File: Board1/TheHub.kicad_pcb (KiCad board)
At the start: 2 copper layers, 118.7 x 184.1 mm, 51 parts, among them J11 RFD900, J12 I2C_1 Test Point, J13 I2C_2 Test Point, J15 GPIO Test, J16 I2C_3 Test Point, J17 12V OUT, J23 NucleoRight, J5 NucleoLeft, J8 12V MAIN POWER, U10 ADXL377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

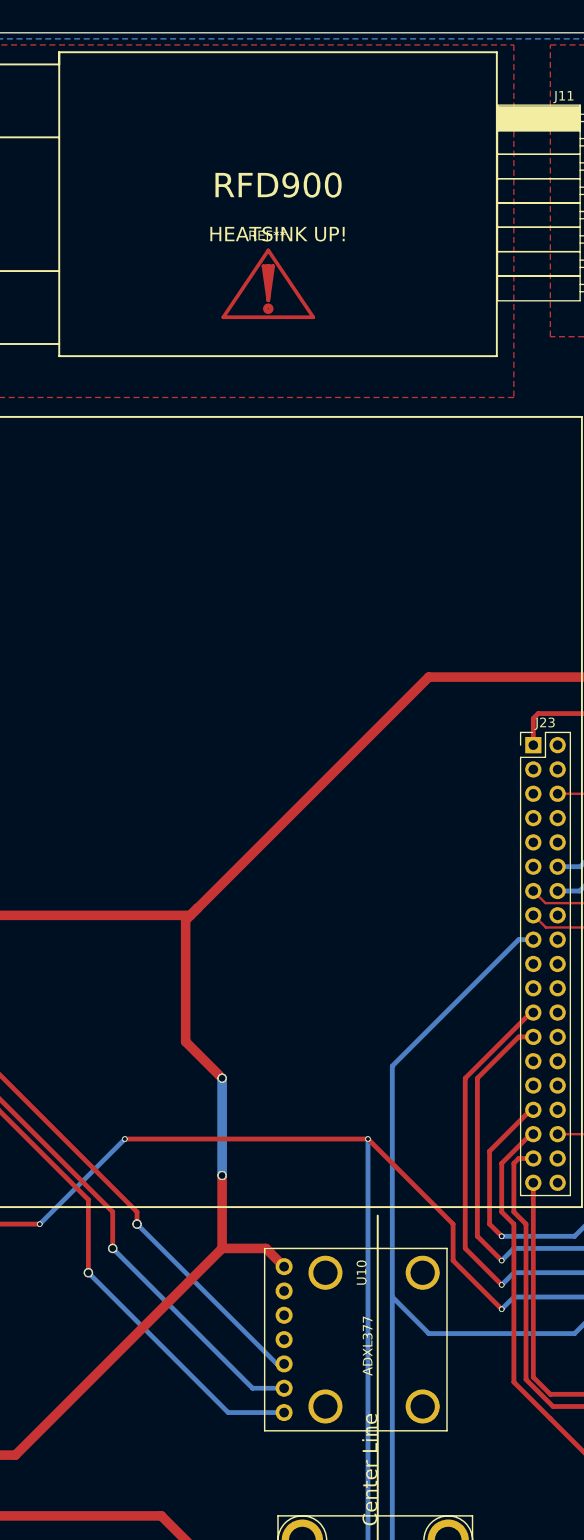
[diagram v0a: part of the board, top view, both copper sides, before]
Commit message: Add mounting points for RFD900
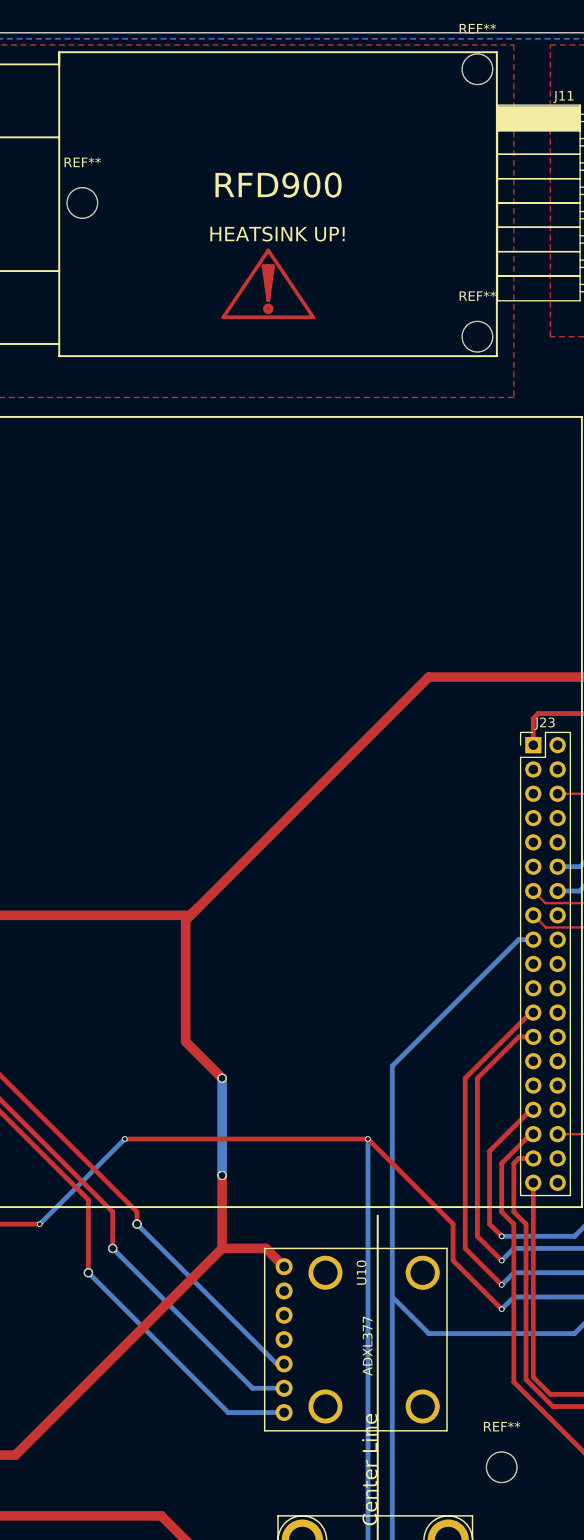
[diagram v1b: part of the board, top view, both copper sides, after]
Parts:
- added REF**: MountingHole_3.2mm_M3, Mounting_Holes:MountingHole_3.2mm_M3, F.Cu at (134.6, 200.7)
- added REF**: MountingHole_3.2mm_M3, Mounting_Holes:MountingHole_3.2mm_M3, F.Cu at (132.1, 82.5)
- added REF**: MountingHole_3.2mm_M3, Mounting_Holes:MountingHole_3.2mm_M3, F.Cu at (132.1, 54.6)
- added REF**: MountingHole_3.2mm_M3, Mounting_Holes:MountingHole_3.2mm_M3, F.Cu at (90.8, 68.6)
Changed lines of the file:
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@@
     (tracks 318)
     (zones 0)
-    (modules 51)
+    (modules 55)
     (nets 107)
   )
@@
     (descr "Symbol, Attention, Copper Top, Small,")
     (tags "Symbol, Attention, Copper Top, Small,")
-    (fp_text reference REF** (at -0.127 -5.715) (layer F.SilkS)
+    (fp_text reference REF** (at 9.144 2.921) (layer F.SilkS) hide
       (effects (font (size 1 1) (thickness 0.15)))
     )
@@
     (pad "" thru_hole circle (at 12.7 -10.16 90) (size 3.5 3.5) (drill 2.55) (layers *.Cu *.Mask))
   )
+  (module Mounting_Holes:MountingHole_3.2mm_M3 (layer F.Cu)
+    (at 134.62 200.66)
+    (descr "Mounting Hole 3.2mm, no annular, M3")
+    (tags "mounting hole 3.2mm no annular m3")
+    (attr virtual)
+    (fp_text reference REF** (at 0 -4.2) (layer F.SilkS)
+      (effects (font (size 1 1) (thickness 0.15)))
+    )
+    (fp_text value MountingHole_3.2mm_M3 (at 0 4.2) (layer F.Fab)
+      (effects (font (size 1 1) (thickness 0.15)))
+    )
+    (fp_text user %R (at 0.3 0) (layer F.Fab)
+      (effects (font (size 1 1) (thickness 0.15)))
+    )
+    (fp_circle (center 0 0) (end 3.2 0) (layer Cmts.User) (width 0.15))
+    (fp_circle (center 0 0) (end 3.45 0) (layer F.CrtYd) (width 0.05))
+    (pad 1 np_thru_hole circle (at 0 0) (size 3.2 3.2) (drill 3.2) (layers *.Cu *.Mask))
+  )
+  (module Mounting_Holes:MountingHole_3.2mm_M3 (layer F.Cu)
+    (at 132.08 82.55)
+    (descr "Mounting Hole 3.2mm, no annular, M3")
+    (tags "mounting hole 3.2mm no annular m3")
+    (attr virtual)
+    (fp_text reference REF** (at 0 -4.2) (layer F.SilkS)
+      (effects (font (size 1 1) (thickness 0.15)))
+    )
+    (fp_text value MountingHole_3.2mm_M3 (at 0 4.2) (layer F.Fab)
+      (effects (font (size 1 1) (thickness 0.15)))
+    )
+    (fp_text user %R (at 0.3 0) (layer F.Fab)
+      (effects (font (size 1 1) (thickness 0.15)))
+    )
+    (fp_circle (center 0 0) (end 3.2 0) (layer Cmts.User) (width 0.15))
+    (fp_circle (center 0 0) (end 3.45 0) (layer F.CrtYd) (width 0.05))
+    (pad 1 np_thru_hole circle (at 0 0) (size 3.2 3.2) (drill 3.2) (layers *.Cu *.Mask))
+  )
+  (module Mounting_Holes:MountingHole_3.2mm_M3 (layer F.Cu)
+    (at 132.08 54.61)
+    (descr "Mounting Hole 3.2mm, no annular, M3")
+    (tags "mounting hole 3.2mm no annular m3")
+    (attr virtual)
+    (fp_text reference REF** (at 0 -4.2) (layer F.SilkS)
+      (effects (font (size 1 1) (thickness 0.15)))
+    )
+    (fp_text value MountingHole_3.2mm_M3 (at 0 4.2) (layer F.Fab)
+      (effects (font (size 1 1) (thickness 0.15)))
+    )
+    (fp_text user %R (at 0.3 0) (layer F.Fab)
+      (effects (font (size 1 1) (thickness 0.15)))
+    )
+    (fp_circle (center 0 0) (end 3.2 0) (layer Cmts.User) (width 0.15))
+    (fp_circle (center 0 0) (end 3.45 0) (layer F.CrtYd) (width 0.05))
+    (pad 1 np_thru_hole circle (at 0 0) (size 3.2 3.2) (drill 3.2) (layers *.Cu *.Mask))
+  )
+  (module Mounting_Holes:MountingHole_3.2mm_M3 (layer F.Cu)
+    (at 90.805 68.58)
+    (descr "Mounting Hole 3.2mm, no annular, M3")
+    (tags "mounting hole 3.2mm no annular m3")
+    (attr virtual)
+    (fp_text reference REF** (at 0 -4.2) (layer F.SilkS)
+      (effects (font (size 1 1) (thickness 0.15)))
+    )
+    (fp_text value MountingHole_3.2mm_M3 (at 0 4.2) (layer F.Fab)
+      (effects (font (size 1 1) (thickness 0.15)))
+    )
+    (fp_text user %R (at 0.3 0) (layer F.Fab)
+      (effects (font (size 1 1) (thickness 0.15)))
+    )
+    (fp_circle (center 0 0) (end 3.2 0) (layer Cmts.User) (width 0.15))
+    (fp_circle (center 0 0) (end 3.45 0) (layer F.CrtYd) (width 0.05))
+    (pad 1 np_thru_hole circle (at 0 0) (size 3.2 3.2) (drill 3.2) (layers *.Cu *.Mask))
+  )
   (gr_text GND (at 164.465 168.275) (layer F.SilkS)

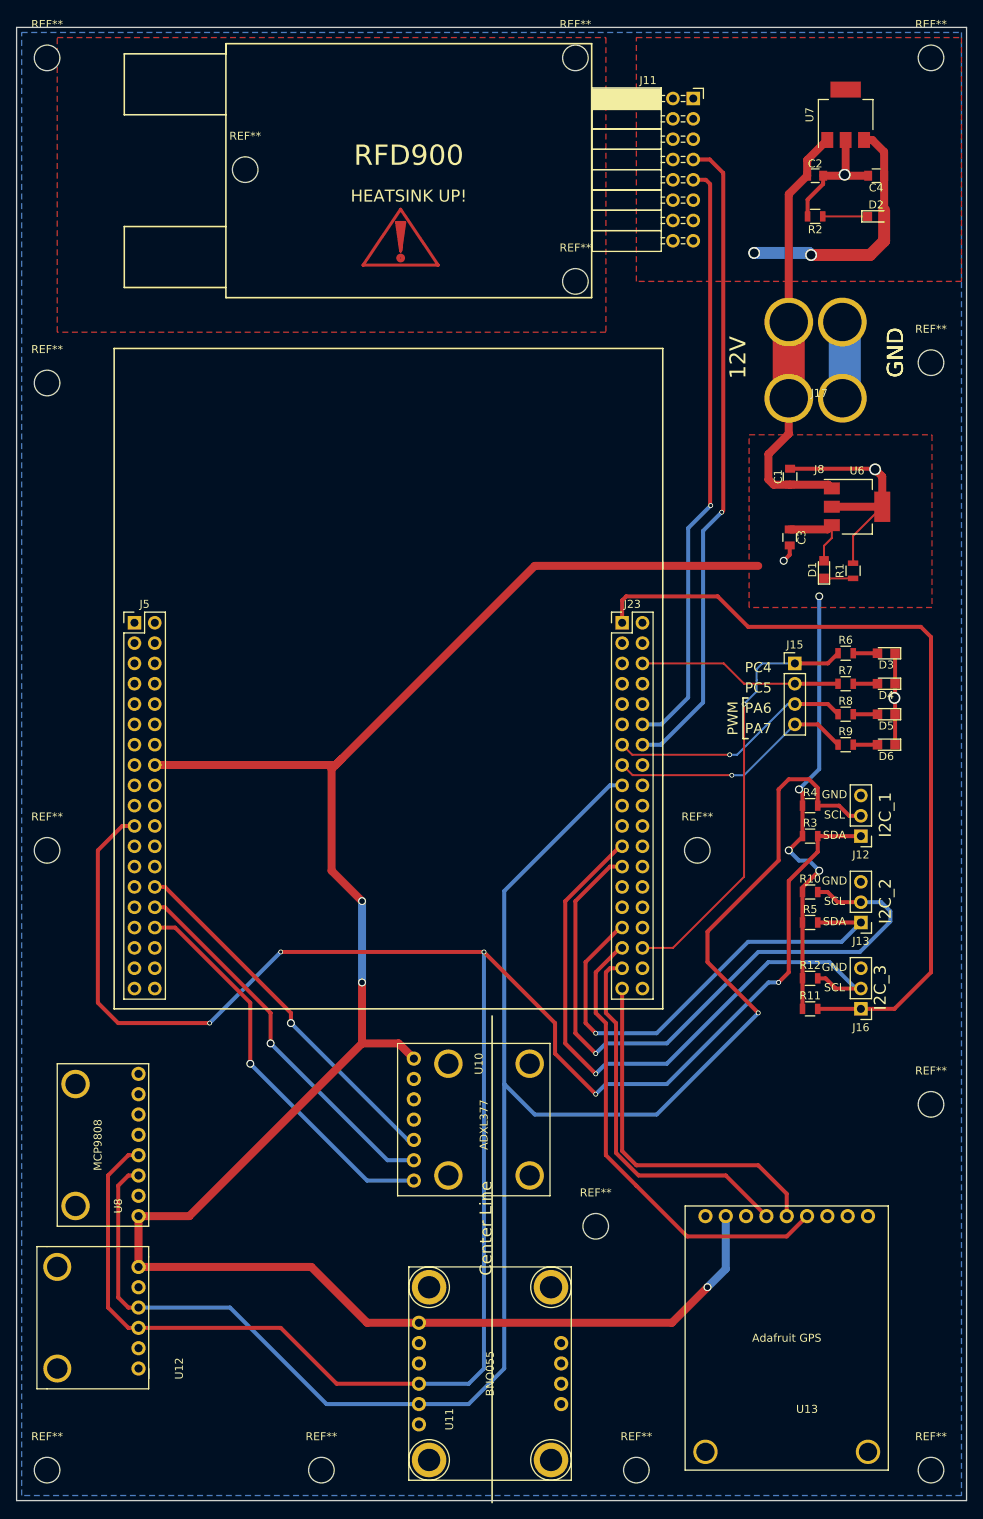
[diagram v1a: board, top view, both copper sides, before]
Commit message: Add Datalogger and RTC to PCB, add I2C addresses to silkscreen
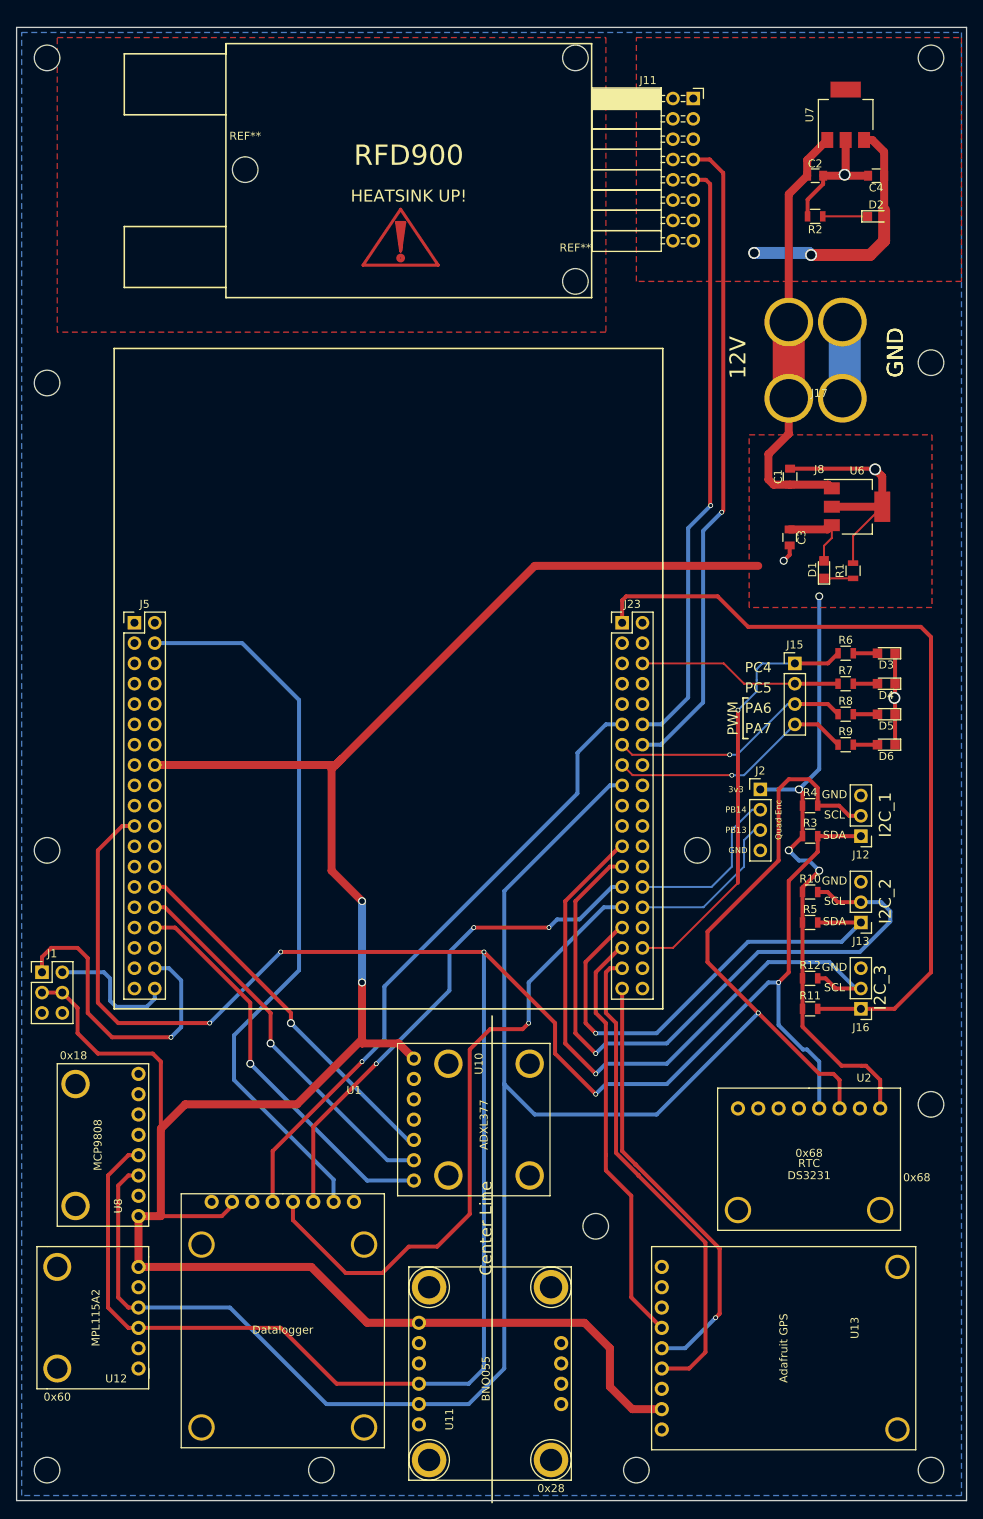
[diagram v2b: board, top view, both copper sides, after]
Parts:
- added J1: Actuator Fdbk Conn, Pin_Headers:Pin_Header_Straight_2x03_Pitch2.54mm, F.Cu at (65.4, 168.9)
- added J2: QuadEnc_Conn, Pin_Headers:Pin_Header_Straight_1x04_Pitch2.54mm, F.Cu at (155.2, 146.1)
- added U1: Datalogger, FoxWestern:Datalogger, F.Cu at (104.4, 197.6)
- added U2: DS3231, FoxWestern:DS3231, F.Cu at (170.2, 185.9)
- moved U13 26.6 mm to (142.9, 205.7), turned to 270 degrees
- renumbered REF** to ?
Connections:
- J5 pad 36: /PC1 -> /A_FDBK_0
- J5 pad 38: /PC0 -> /A_FDBK_1
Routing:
- net /PD2: track 0.00 -> 92.2 mm
- net /PB5: track 0.00 -> 80.1 mm, vias 0 -> 1
- net /PA5: track 0.00 -> 79.0 mm, vias 0 -> 1
- net +3V3: track 326.7 -> 396.3 mm, vias 7 -> 6
- net /PB4: track 0.00 -> 63.2 mm, vias 0 -> 3
- net /A_FDBK_0: track 0.00 -> 38.7 mm, vias 0 -> 1
- net /PB14: track 0.00 -> 21.4 mm
- net /PB13: track 0.00 -> 20.7 mm
- net /PB7: track 281.3 -> 299.4 mm
- net /PB6: track 239.4 -> 256.6 mm
- net /A_FDBK_1: track 0.00 -> 16.7 mm
- net /PA2: track 47.4 -> 61.2 mm
- net /PA3: track 45.9 -> 54.9 mm, vias 0 -> 1
- net /GPS_FIX: track 58.4 -> 52.4 mm
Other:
- board text added: "0x18"
- board text added: "0x28"
- board text added: "0x60"
- board text added: "0x68"
- board text added: "3v3"
- board text added: "MPL115A2"
- board text added: "PB13"
- board text added: "PB14"
- board text added: "Quad Enc"

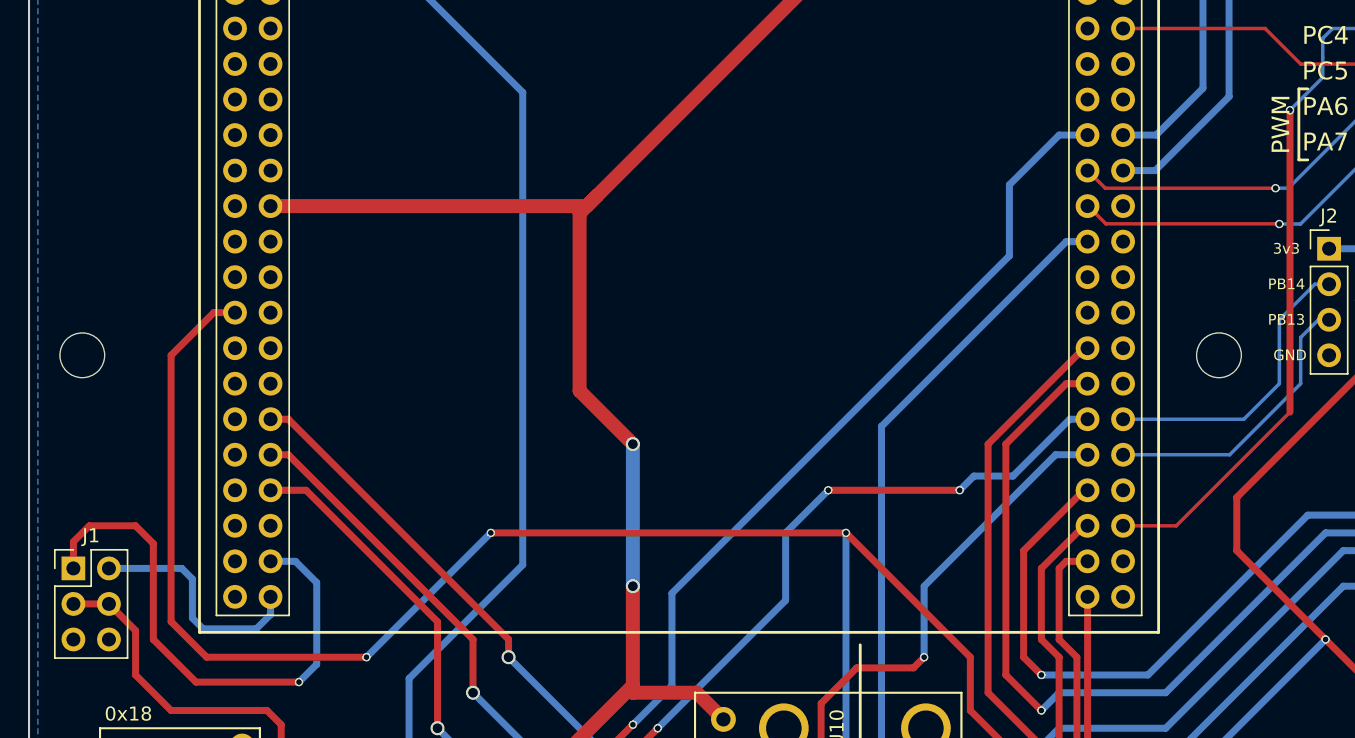
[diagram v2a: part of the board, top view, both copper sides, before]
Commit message: Add silkscreen lables for RX, TX, Nucleo, and analog feedback
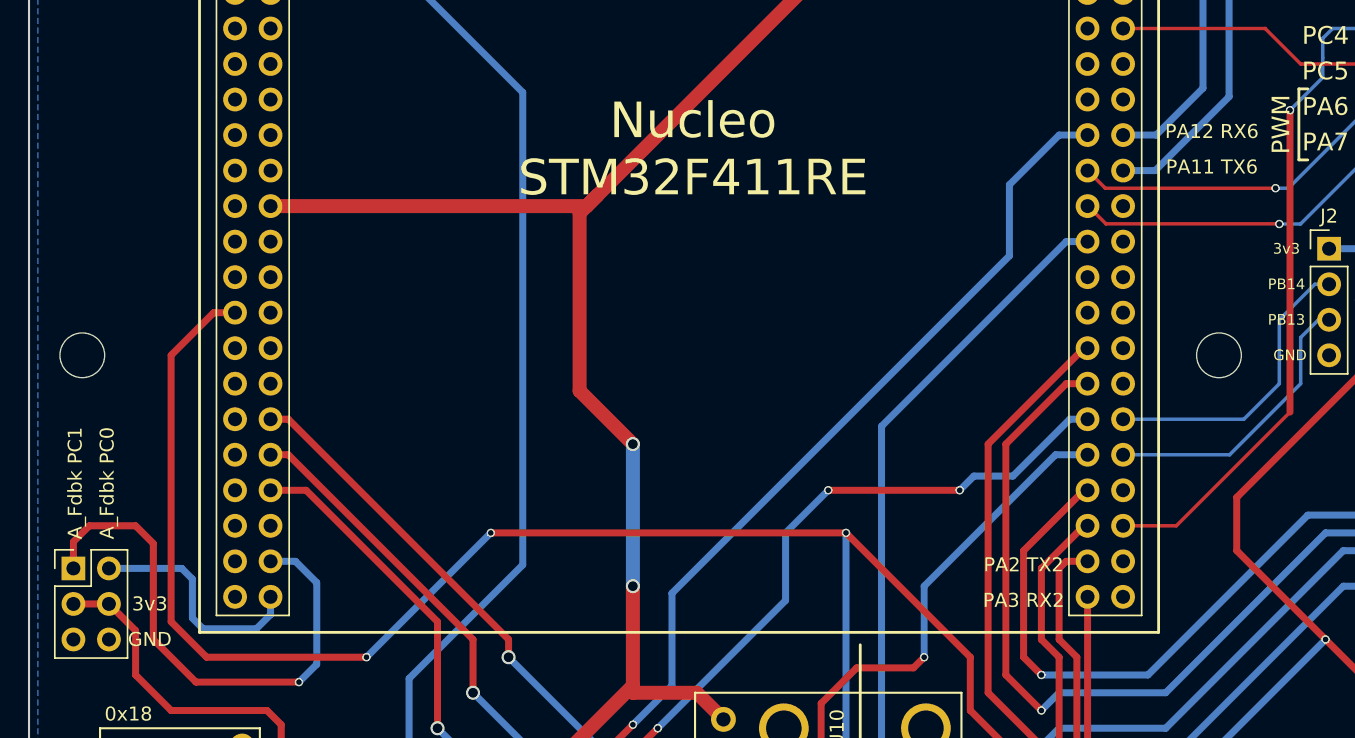
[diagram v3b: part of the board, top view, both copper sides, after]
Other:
- board text added: "A_Fdbk PC0"
- board text added: "A_Fdbk PC1"
- board text added: "Nucleo STM32F411RE"
- board text added: "PA11 TX6"
- board text added: "PA12 RX6"
- board text added: "PA2 TX2"
- board text added: "PA3 RX2"
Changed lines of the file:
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@@
     (area 62.154999 50.724999 181.050001 235.025001)
     (thickness 1.6)
-    (drawings 59)
+    (drawings 68)
     (tracks 429)
     (zones 0)
@@
     (descr "Through hole straight pin header, 2x03, 2.54mm pitch, double rows")
     (tags "Through hole pin header THT 2x03 2.54mm double row")
-    (fp_text reference J1 (at 1.27 -2.33) (layer F.SilkS)
+    (fp_text reference J1 (at 1.27 -2.33) (layer F.SilkS) hide
       (effects (font (size 1 1) (thickness 0.15)))
     )
@@
     (pad "" thru_hole circle (at 0 -12.7 180) (size 3.302 3.302) (drill 2.54) (layers *.Cu *.Mask))
   )
+  (gr_text "PA2 TX2" (at 133.35 168.656) (layer F.SilkS)
+    (effects (font (size 1 1) (thickness 0.15)))
+  )
+  (gr_text "PA3 RX2" (at 133.35 171.196) (layer F.SilkS)
+    (effects (font (size 1 1) (thickness 0.15)))
+  )
+  (gr_text "PA11 TX6" (at 146.812 140.208) (layer F.SilkS)
+    (effects (font (size 1 1) (thickness 0.15)))
+  )
+  (gr_text "PA12 RX6" (at 146.812 137.668) (layer F.SilkS)
+    (effects (font (size 1 1) (thickness 0.15)))
+  )
+  (gr_text "Nucleo\nSTM32F411RE" (at 109.728 138.938) (layer F.SilkS)
+    (effects (font (size 2.54 2.54) (thickness 0.508)))
+  )
+  (gr_text GND (at 70.866 173.99) (layer F.SilkS)
+    (effects (font (size 1 1) (thickness 0.15)))
+  )
+  (gr_text 3v3 (at 70.866 171.45) (layer F.SilkS)
+    (effects (font (size 1 1) (thickness 0.15)))
+  )
+  (gr_text "A_Fdbk PC0" (at 67.818 162.814 90) (layer F.SilkS)
+    (effects (font (size 1 1) (thickness 0.15)))
+  )
+  (gr_text "A_Fdbk PC1" (at 65.532 162.814 90) (layer F.SilkS)
+    (effects (font (size 1 1) (thickness 0.15)))
+  )
   (gr_text 0x68 (at 174.752 194.564) (layer F.SilkS)
